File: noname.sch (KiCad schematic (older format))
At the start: 24 parts, among them P1 CONN_01X07, U1 MSP430G2955IRHA40, U3 RT9193

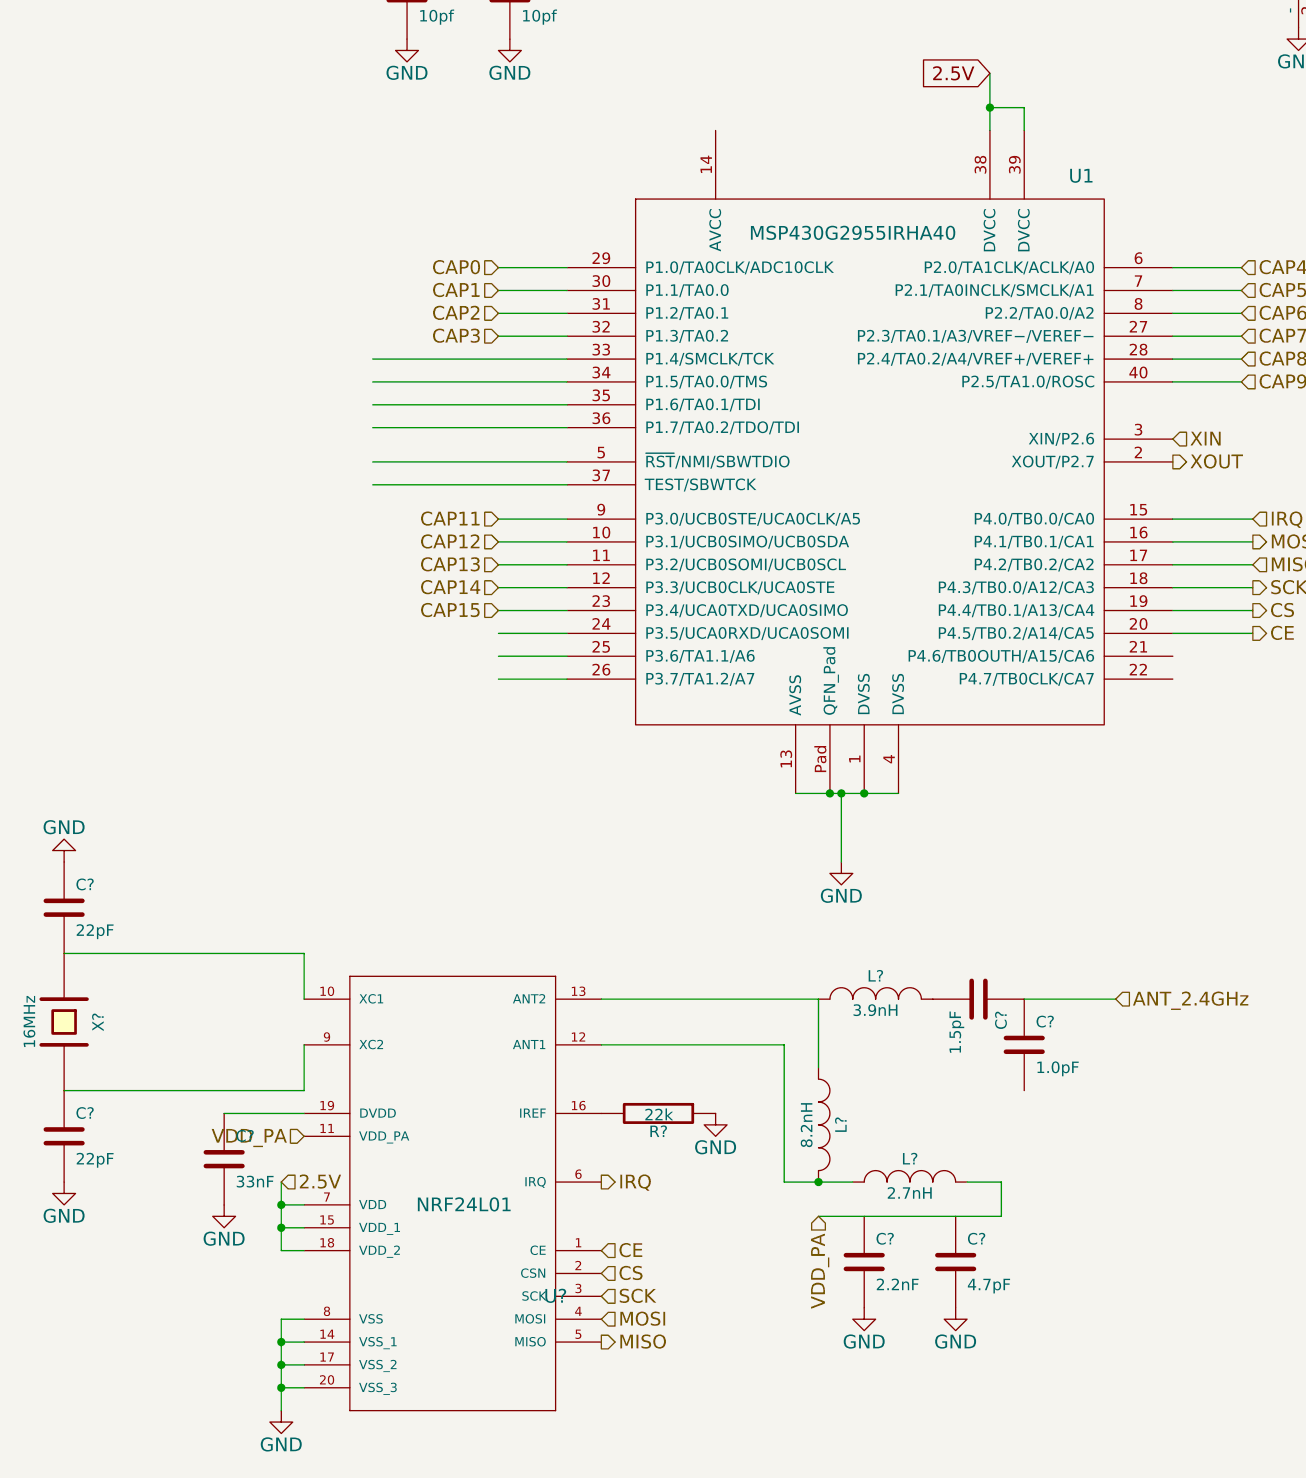
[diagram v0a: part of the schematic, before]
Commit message: Added capacitor footprints
mostly 0402s for the radio
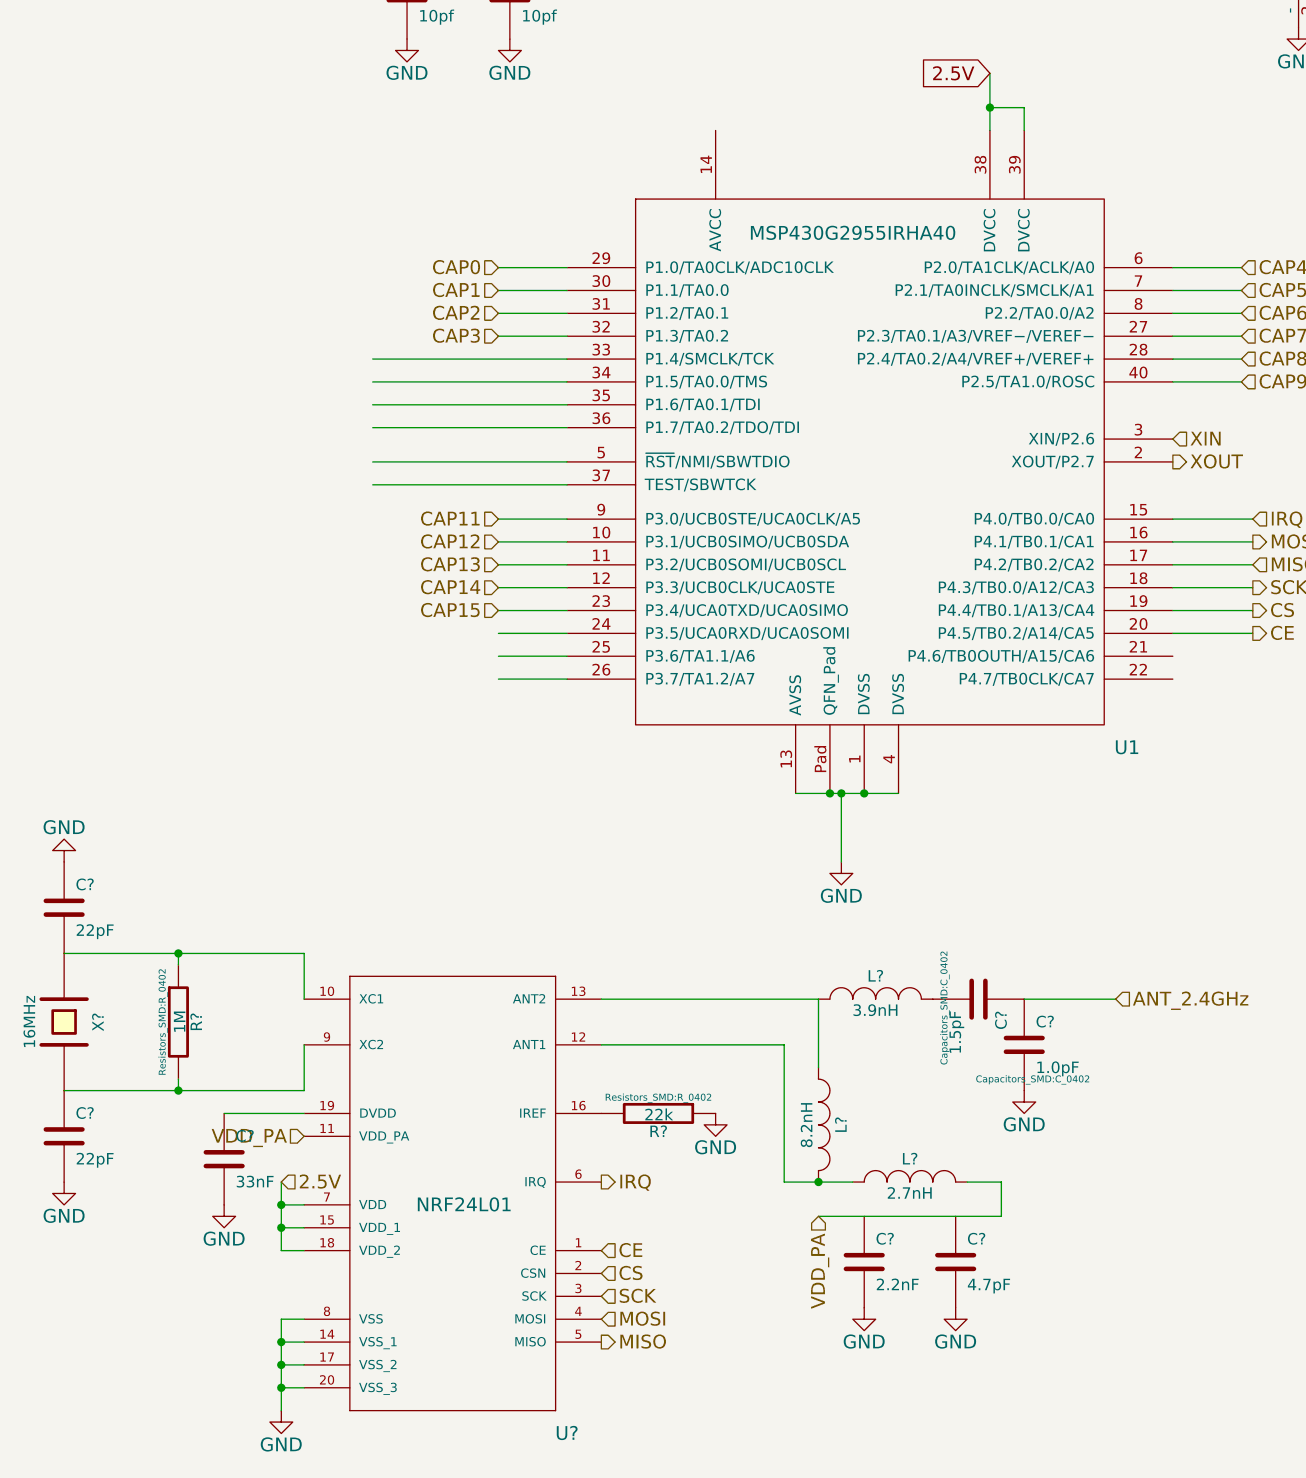
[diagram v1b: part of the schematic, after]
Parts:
- added R?: 1M, Resistors_SMD:R_0402, symbol R
- C? (x7), L? (x3): footprint (none) -> Capacitors_SMD:C_0402
- R?: footprint (none) -> Resistors_SMD:R_0402
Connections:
- wire segments 86 -> 88
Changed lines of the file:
@@
 U 1 1 54F240CC
 P 3600 2150
-F 0 "U1" H 5550 2250 60  0000 C CNN
+F 0 "U1" H 5750 -250 60  0000 C CNN
 F 1 "MSP430G2955IRHA40" H 4550 2000 60  0000 C CNN
 F 2 "" H 550 1650 60  0000 C CNN
@@
 U 1 1 54F3687D
 P 2850 6550
-F 0 "U?" H 3250 6150 60  0000 C CNN
+F 0 "U?" H 3300 5550 60  0000 C CNN
 F 1 "NRF24L01" H 2850 6550 60  0000 C CNN
 F 2 "" H 3250 6150 60  0000 C CNN
@@
 F 0 "C?" H 1850 6450 50  0000 L CNN
 F 1 "33nF" H 1850 6250 50  0000 L CNN
-F 2 "" H 1838 6200 30  0000 C CNN
+F 2 "Capacitors_SMD:C_0402" H 1838 6200 30  0001 C CNN
 F 3 "" H 1800 6350 60  0000 C CNN
 	1    1800 6350
@@
 F 0 "C?" H 1150 5350 50  0000 L CNN
 F 1 "22pF" H 1150 5150 50  0000 L CNN
-F 2 "" H 1138 5100 30  0000 C CNN
+F 2 "Capacitors_SMD:C_0402" H 1138 5100 30  0001 C CNN
 F 3 "" H 1100 5250 60  0000 C CNN
 	1    1100 5250
@@
 F 0 "C?" H 1150 6350 50  0000 L CNN
 F 1 "22pF" H 1150 6150 50  0000 L CNN
-F 2 "" H 1138 6100 30  0000 C CNN
+F 2 "Capacitors_SMD:C_0402" H 1138 6100 30  0001 C CNN
 F 3 "" H 1100 6250 60  0000 C CNN
 	1    1100 6250
@@
 F 0 "L?" H 4650 5750 50  0000 C CNN
 F 1 "3.9nH" H 4650 5600 50  0000 C CNN
-F 2 "" H 4650 5650 60  0000 C CNN
+F 2 "Capacitors_SMD:C_0402" H 4650 5650 60  0001 C CNN
 F 3 "" H 4650 5650 60  0000 C CNN
 	1    4650 5650
@@
 F 0 "L?" H 4400 6300 50  0000 C CNN
 F 1 "8.2nH" H 4400 6150 50  0000 C CNN
-F 2 "" H 4400 6200 60  0000 C CNN
+F 2 "Capacitors_SMD:C_0402" H 4400 6200 60  0001 C CNN
 F 3 "" H 4400 6200 60  0000 C CNN
 	1    4400 6200
@@
 F 0 "L?" H 4800 6550 50  0000 C CNN
 F 1 "2.7nH" H 4800 6400 50  0000 C CNN
-F 2 "" H 4800 6450 60  0000 C CNN
+F 2 "Capacitors_SMD:C_0402" H 4800 6450 60  0001 C CNN
 F 3 "" H 4800 6450 60  0000 C CNN
 	1    4800 6450
@@
 F 0 "C?" H 4650 6900 50  0000 L CNN
 F 1 "2.2nF" H 4650 6700 50  0000 L CNN
-F 2 "" H 4638 6650 30  0000 C CNN
+F 2 "Capacitors_SMD:C_0402" H 4638 6650 30  0001 C CNN
 F 3 "" H 4600 6800 60  0000 C CNN
 	1    4600 6800
@@
 F 0 "C?" H 5050 6900 50  0000 L CNN
 F 1 "4.7pF" H 5050 6700 50  0000 L CNN
-F 2 "" H 5038 6650 30  0000 C CNN
+F 2 "Capacitors_SMD:C_0402" H 5038 6650 30  0001 C CNN
 F 3 "" H 5000 6800 60  0000 C CNN
 	1    5000 6800
@@
 F 0 "C?" H 5150 5750 50  0000 L CNN
 F 1 "1.5pF" H 5150 5550 50  0000 L CNN
-F 2 "" H 5138 5500 30  0000 C CNN
+F 2 "Capacitors_SMD:C_0402" H 5138 5500 30  0000 C CNN
 F 3 "" H 5100 5650 60  0000 C CNN
 	1    5100 5650
@@
 F 0 "C?" H 5350 5950 50  0000 L CNN
 F 1 "1.0pF" H 5350 5750 50  0000 L CNN
-F 2 "" H 5338 5700 30  0000 C CNN
+F 2 "Capacitors_SMD:C_0402" H 5338 5700 30  0000 C CNN
 F 3 "" H 5300 5850 60  0000 C CNN
 	1    5300 5850
@@
 F 0 "R?" V 3780 6150 50  0000 C CNN
 F 1 "22k" V 3707 6151 50  0000 C CNN
-F 2 "" V 3630 6150 30  0000 C CNN
+F 2 "Resistors_SMD:R_0402" V 3630 6150 30  0000 C CNN
 F 3 "" H 3700 6150 30  0000 C CNN
 	1    3700 6150
@@
 Text HLabel 5950 3300 2    60   Output ~ 0
 XOUT
+$Comp
+L R R?
+U 1 1 54F3D0B5
+P 1600 5750
+F 0 "R?" V 1680 5750 50  0000 C CNN
+F 1 "1M" V 1607 5751 50  0000 C CNN
+F 2 "Resistors_SMD:R_0402" V 1530 5750 30  0000 C CNN
+F 3 "" H 1600 5750 30  0000 C CNN
+	1    1600 5750
+	1    0    0    -1
+$EndComp
+Wire Wire Line
+	1600 5500 1600 5450
+Connection ~ 1600 5450
+Wire Wire Line
+	1600 6000 1600 6050
+Connection ~ 1600 6050
+$Comp
+L GND #PWR?
+U 1 1 54F3D939
+P 5300 6050
+F 0 "#PWR?" H 5300 5800 60  0001 C CNN
+F 1 "GND" H 5300 5900 60  0000 C CNN
+F 2 "" H 5300 6050 60  0000 C CNN
+F 3 "" H 5300 6050 60  0000 C CNN
+	1    5300 6050
+	1    0    0    -1
+$EndComp
 $EndSCHEMATC
